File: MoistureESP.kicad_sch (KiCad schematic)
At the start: 0 parts

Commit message: Batter scematic done.
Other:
- sheet battery ports: added Vcell+, Vcell-, Vpack+, Vpack-, comm{I2C}; removed Vpack
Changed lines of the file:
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@@
 			)
 		)
-		(pin "Vpack" input
-			(at 88.9 72.39 0)
+		(pin "Vpack-" output
+			(at 88.9 82.55 0)
 			(effects
 				(font
+					(size 1.27 1.27)
+				)
+				(justify right)
+			)
+		)
+		(pin "Vcell+" input
+			(at 50.8 69.85 180)
+			(effects
+				(font
+					(size 1.27 1.27)
+				)
+				(justify left)
+			)
+		)
+		(pin "Vcell-" input
+			(at 50.8 82.55 180)
+			(effects
+				(font
+					(size 1.27 1.27)
+				)
+				(justify left)
+			)
+		)
+		(pin "comm{I2C}" bidirectional
+			(at 76.2 88.9 270)
+			(effects
+				(font
+					(size 1.27 1.27)
+				)
+				(justify left)
+			)
+		)
+		(pin "Vpack+" output
+			(at 88.9 69.85 0)
+			(effects
+				(font

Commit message: Draw power schematic.
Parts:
- added JP1: Jumper_2_Bridged, Connector_PinHeader_2.54mm:PinHeader_1x02_P2.54mm_Horizontal, symbol Jumper:Jumper_2_Bridged
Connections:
- new net mcu/VDD: JP1.2 (B)
- new net power/Vout+: JP1.1 (A)
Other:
- sheet mcu ports: added 1-Wire_pin, ADC_pin, Battery{I2C}, Disp{I2C}, MCU{UART}, Sensor_enable, VDD, VSS; removed none
- sheet power ports: added Vin+, Vin-, Vout+, Vout-; removed none

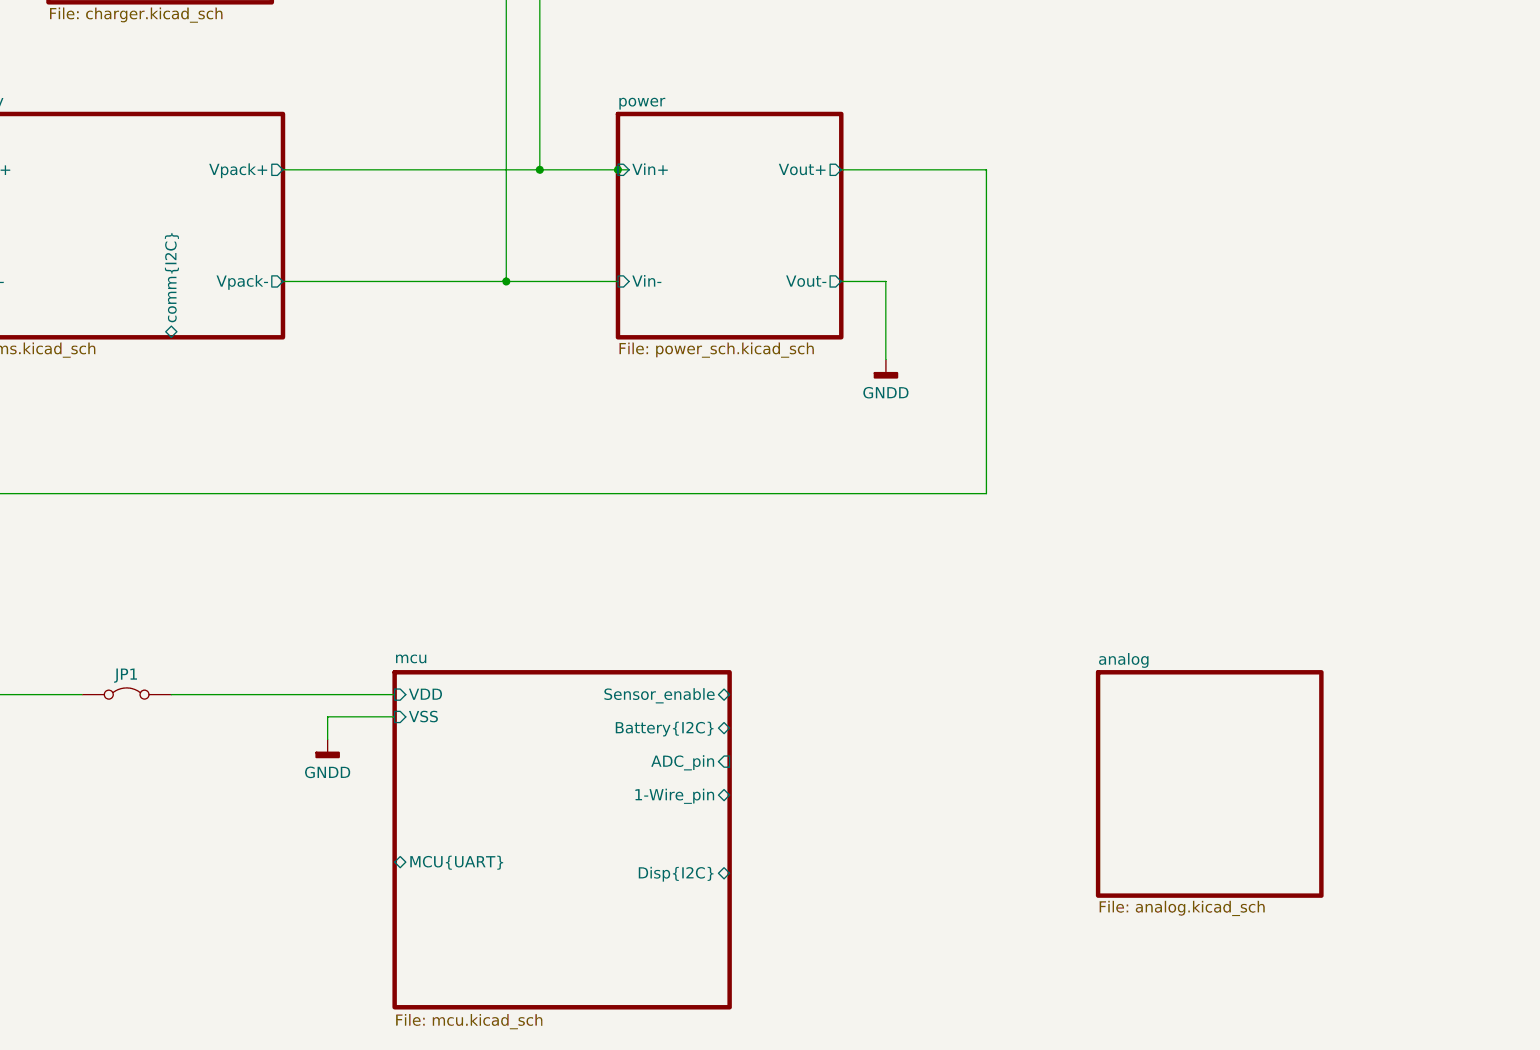
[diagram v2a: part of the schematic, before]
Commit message: Change BJT to FET in MCU. Add pinout.
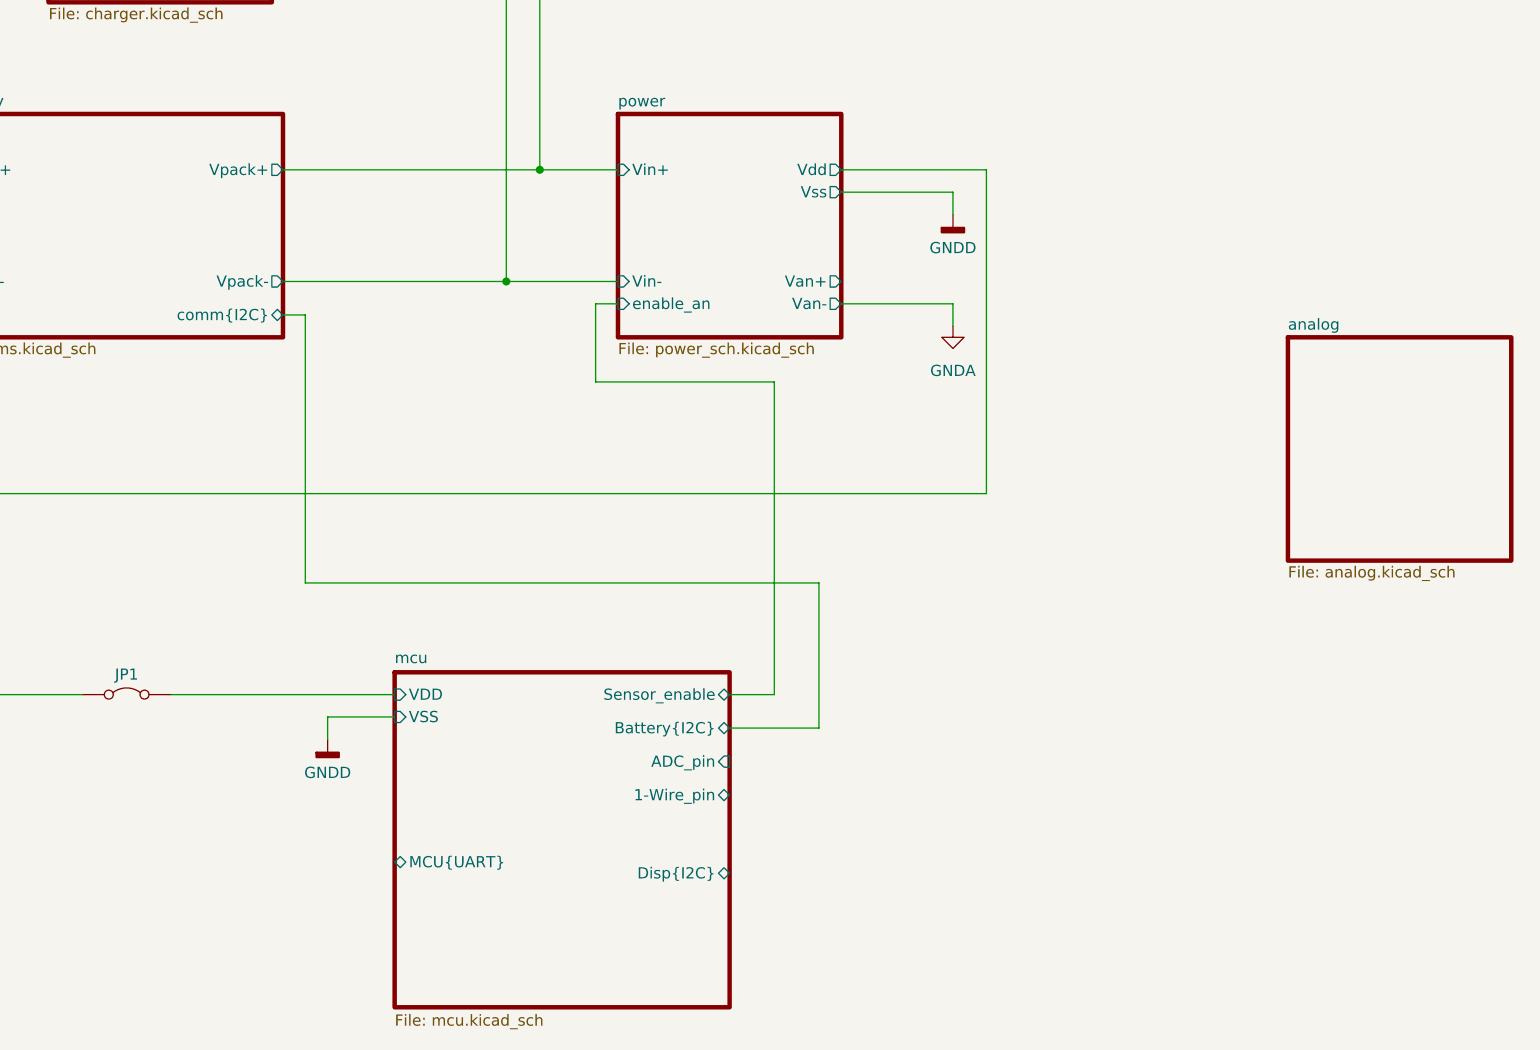
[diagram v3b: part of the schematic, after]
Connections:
- net power/Vout+ renamed power/Vdd
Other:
- sheet power ports: added Van+, Van-, Vdd, Vss, enable_an; removed Vout+, Vout-
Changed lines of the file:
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@@
 		(color 0 0 0 0)
 	)
-	(junction
-		(at 127 69.85)
-		(diameter 0)
-		(color 0 0 0 0)
+	(wire
+		(pts
+			(xy 91.44 86.36) (xy 91.44 116.84)
+		)
+		(stroke
+			(width 0)
+			(type default)
+		)
 	)
 	(wire
@@
 	(wire
 		(pts
-			(xy 157.48 82.55) (xy 157.48 91.44)
+			(xy 144.78 129.54) (xy 144.78 93.98)
+		)
+		(stroke
+			(width 0)
+			(type default)
+		)
+	)
+	(wire
+		(pts
+			(xy 124.46 93.98) (xy 124.46 85.09)
+		)
+		(stroke
+			(width 0)
+			(type default)
+		)
+	)
+	(wire
+		(pts
+			(xy 165.1 72.39) (xy 165.1 74.93)
 		)
 		(stroke
@@
 	(wire
 		(pts
+			(xy 139.7 129.54) (xy 144.78 129.54)
+		)
+		(stroke
+			(width 0)
+			(type default)
+		)
+	)
+	(wire
+		(pts
+			(xy 144.78 93.98) (xy 124.46 93.98)
+		)
+		(stroke
+			(width 0)
+			(type default)
+		)
+	)
+	(wire
+		(pts
 			(xy 114.3 82.55) (xy 127 82.55)
 		)
@@
 	(wire
 		(pts
+			(xy 91.44 116.84) (xy 149.86 116.84)
+		)
+		(stroke
+			(width 0)
+			(type default)
+		)
+	)
+	(wire
+		(pts
+			(xy 165.1 87.63) (xy 165.1 85.09)
+		)
+		(stroke
+			(width 0)
+			(type default)
+		)
+	)
+	(wire
+		(pts
+			(xy 88.9 86.36) (xy 91.44 86.36)
+		)
+		(stroke
+			(width 0)
+			(type default)
+		)
+	)
+	(wire
+		(pts
 			(xy 66.04 129.54) (xy 49.53 129.54)
 		)
@@
 	(wire
 		(pts
+			(xy 124.46 85.09) (xy 127 85.09)
+		)
+		(stroke
+			(width 0)
+			(type default)
+		)
+	)
+	(wire
+		(pts
 			(xy 76.2 129.54) (xy 101.6 129.54)
 		)
@@
 	(wire
 		(pts
+			(xy 149.86 116.84) (xy 149.86 133.35)
+		)
+		(stroke
+			(width 0)
+			(type default)
+		)
+	)
+	(wire
+		(pts
 			(xy 49.53 106.68) (xy 168.91 106.68)
 		)
@@
 	(wire
 		(pts
+			(xy 165.1 85.09) (xy 152.4 85.09)
+		)
+		(stroke
+			(width 0)
+			(type default)
+		)
+	)
+	(wire
+		(pts
 			(xy 118.11 31.75) (xy 118.11 69.85)
 		)
@@
 	(wire
 		(pts
+			(xy 149.86 133.35) (xy 139.7 133.35)
+		)
+		(stroke
+			(width 0)
+			(type default)
+		)
+	)
+	(wire
+		(pts
 			(xy 101.6 132.08) (xy 93.98 132.08)
 		)
@@
 	(wire
 		(pts
-			(xy 127 69.85) (xy 128.27 69.85)
-		)
-		(stroke
-			(width 0)
-			(type default)
-		)
-	)
-	(wire
-		(pts
 			(xy 114.3 45.72) (xy 114.3 82.55)
 		)
@@
 	(wire
 		(pts
-			(xy 152.4 82.55) (xy 157.48 82.55)
+			(xy 152.4 72.39) (xy 165.1 72.39)
 		)
 		(stroke
@@
 	(symbol
 		(lib_id "power:GNDD")
-		(at 157.48 91.44 0)
+		(at 165.1 74.93 0)
 		(unit 1)
 		(body_style 1)
@@
 		(fields_autoplaced yes)
 		(property "Reference" "#PWR016"
-			(at 157.48 97.79 0)
+			(at 165.1 81.28 0)
 			(hide yes)
 			(show_name no)
@@
 		)
 		(property "Value" "GNDD"
-			(at 157.48 95.25 0)
+			(at 165.1 78.74 0)
 			(show_name no)
 			(do_not_autoplace no)
@@
 		)
 		(property "Footprint" ""
-			(at 157.48 91.44 0)
+			(at 165.1 74.93 0)
 			(hide yes)
 			(show_name no)
@@
 		)
 		(property "Datasheet" ""
-			(at 157.48 91.44 0)
+			(at 165.1 74.93 0)
 			(hide yes)
 			(show_name no)
@@
 		)
 		(property "Description" "Power symbol creates a global label with name \"GNDD\" , digital ground"
-			(at 157.48 91.44 0)
+			(at 165.1 74.93 0)
 			(hide yes)
 			(show_name no)
@@
 		)
 	)
+	(symbol
+		(lib_id "power:GNDA")
+		(at 165.1 87.63 0)
+		(unit 1)
+		(body_style 1)
+		(exclude_from_sim no)
+		(in_bom yes)
+		(on_board yes)
+		(in_pos_files yes)
+		(dnp no)
+		(fields_autoplaced yes)
+		(property "Reference" "#PWR031"
+			(at 165.1 93.98 0)
+			(hide yes)
+			(show_name no)
+			(do_not_autoplace no)
+			(effects
+				(font
+					(size 1.27 1.27)
+				)
+			)
+		)
+		(property "Value" "GNDA"
+			(at 165.1 92.71 0)
+			(show_name no)
+			(do_not_autoplace no)
+			(effects
+				(font
+					(size 1.27 1.27)
+				)
+			)
+		)
+		(property "Footprint" ""
+			(at 165.1 87.63 0)
+			(hide yes)
+			(show_name no)
+			(do_not_autoplace no)
+			(effects
+				(font
+					(size 1.27 1.27)
+				)
+			)
+		)
+		(property "Datasheet" ""
+			(at 165.1 87.63 0)
+			(hide yes)
+			(show_name no)
+			(do_not_autoplace no)
+			(effects
+				(font
+					(size 1.27 1.27)
+				)
+			)
+		)
+		(property "Description" "Power symbol creates a global label with name \"GNDA\" , analog ground"
+			(at 165.1 87.63 0)
+			(hide yes)
+			(show_name no)
+			(do_not_autoplace no)
+			(effects
+				(font
+					(size 1.27 1.27)
+				)
+			)
+		)
+		(pin "1"
+		)
+		(instances
+			(project "MoistureESP"
+				(path "/f2b9f638-139e-46ec-aa60-77c4af989196"
+					(reference "#PWR031")
+					(unit 1)
+				)
+			)
+		)
+	)
 	(sheet
 		(at 101.6 127)
@@
 			)
 		)
-		(pin "Vout-" output
+		(pin "Vss" output
+			(at 152.4 72.39 0)
+			(effects
+				(font
+					(size 1.27 1.27)
+				)
+				(justify right)
+			)
+		)
+		(pin "enable_an" input
+			(at 127 85.09 180)
+			(effects
+				(font
+					(size 1.27 1.27)
+				)
+				(justify left)
+			)
+		)
+		(pin "Van-" output
+			(at 152.4 85.09 0)
+			(effects
+				(font
+					(size 1.27 1.27)
+				)
+				(justify right)
+			)
+		)
+		(pin "Van+" output
 			(at 152.4 82.55 0)
 			(effects
@@
 			)
 		)
-		(pin "Vout+" output
+		(pin "Vdd" output
 			(at 152.4 69.85 0)
 			(effects
@@
 	)
 	(sheet
-		(at 181.61 127)
+		(at 203.2 88.9)
 		(size 25.4 25.4)
 		(exclude_from_sim no)
@@
 		)
 		(property "Sheetname" "analog"
-			(at 181.61 126.2884 0)
+			(at 203.2 88.1884 0)
 			(show_name no)
 			(do_not_autoplace no)
@@
 		)
 		(property "Sheetfile" "analog.kicad_sch"
-			(at 181.61 152.9846 0)
+			(at 203.2 114.8846 0)
 			(show_name no)
 			(do_not_autoplace no)
@@
 		)
 		(pin "comm{I2C}" bidirectional
-			(at 76.2 88.9 270)
-			(effects
-				(font
-					(size 1.27 1.27)
-				)
-				(justify left)
-			)
-		)
+			(at 88.9 86.36 0)
+			(effects
+				(font
+					(size 1.27 1.27)
+				)
+				(justify right)
+			)
+		)

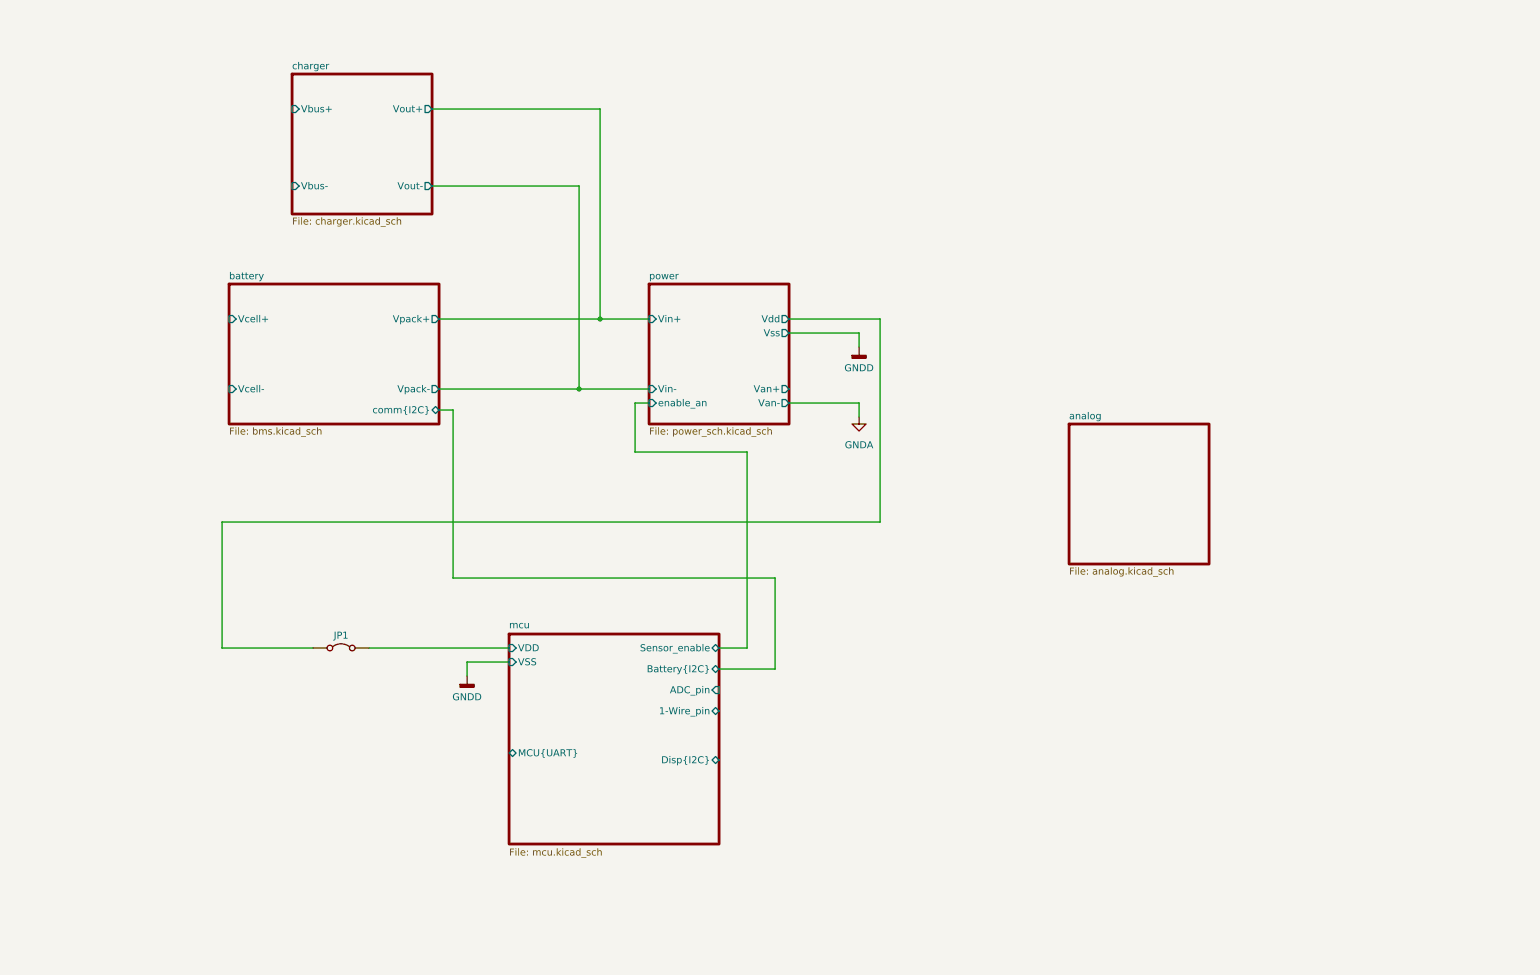
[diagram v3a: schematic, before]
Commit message: Add analog schematic and refine wiring on top.
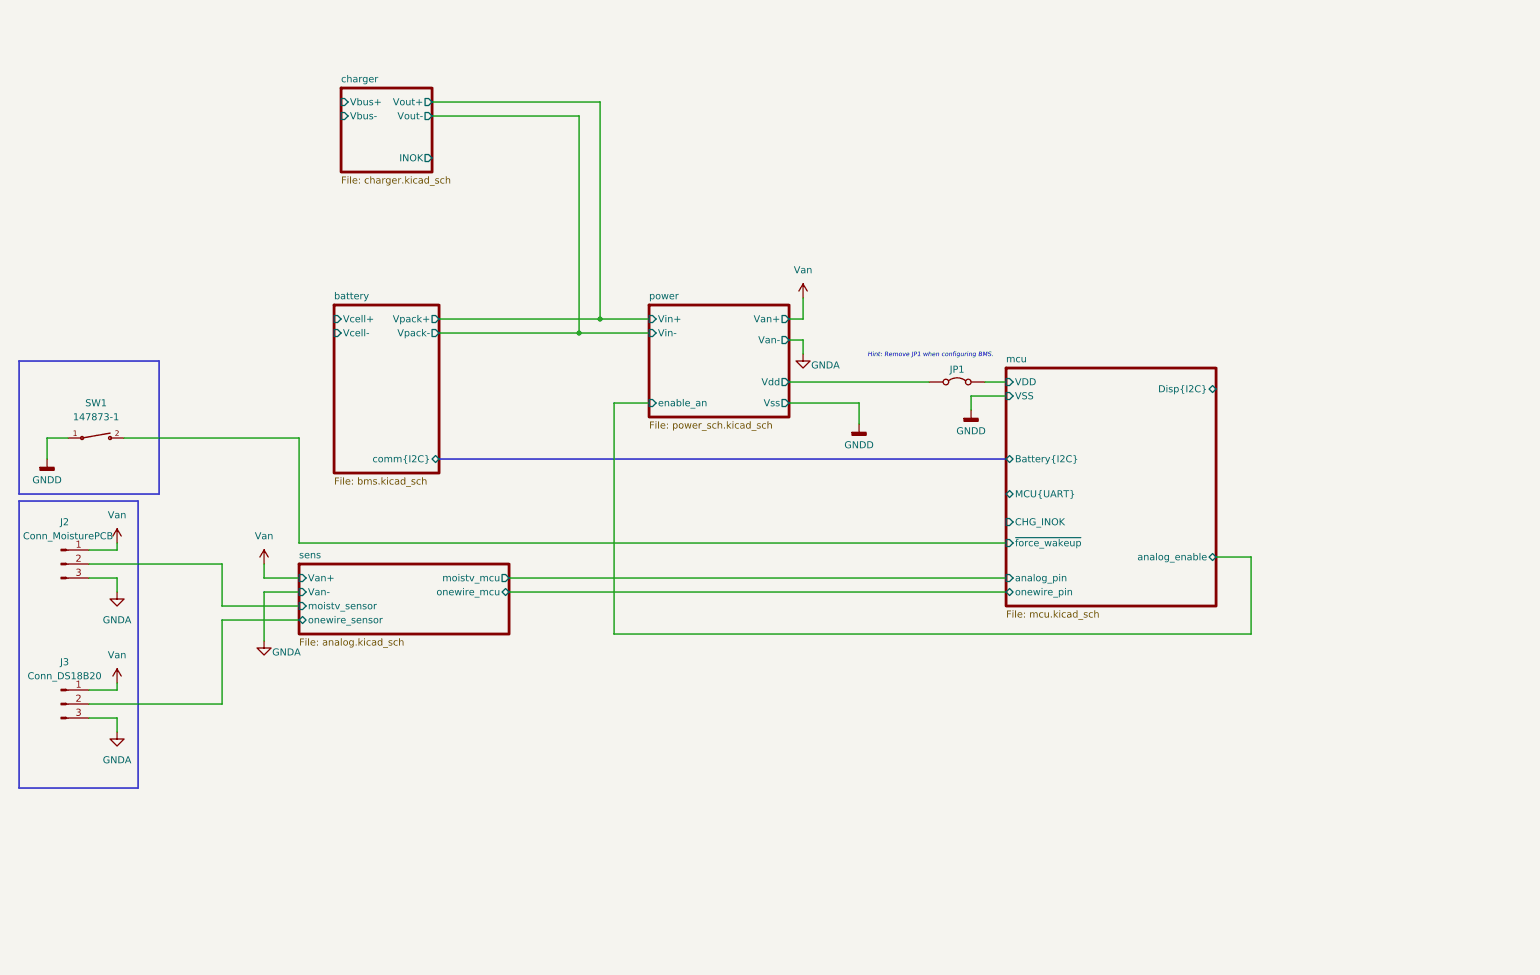
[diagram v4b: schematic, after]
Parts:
- added J2: Conn_MoisturePCB, custom:sensorwirepads3x1, symbol Connector:Conn_01x03_Pin
- added J3: Conn_DS18B20, custom:sensorwirepads3x1, symbol Connector:Conn_01x03_Pin
- added SW1: 147873-1, custom:SW_147873-1, symbol custom:147873-1
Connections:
- net GNDA: now also J2.3 (Pin_3), J3.3 (Pin_3)
- net GNDD: now also SW1.1
- new net Van: J2.1 (Pin_1), J3.1 (Pin_1)
- new net mcu/~{force_wakeup}: SW1.2
- new net sens/moistv_sensor: J2.2 (Pin_2)
- new net sens/onewire_sensor: J3.2 (Pin_2)
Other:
- sheet analog renamed sens
- sheet charger ports: added INOK; removed none
- sheet mcu ports: added CHG_INOK, analog_enable, analog_pin, onewire_pin, ~{force_wakeup}; removed 1-Wire_pin, ADC_pin, Sensor_enable
- sheet sens ports: added Van+, Van-, moistv_mcu, moistv_sensor, onewire_mcu, onewire_sensor; removed none
- note added: "Hint: Remove JP1 when configuring BMS."
- moved on the sheet: JP1
